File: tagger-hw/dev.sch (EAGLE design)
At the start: 50 parts, among them J2 22-23-2021, J3 22-23-2021, X1 EXC-31B

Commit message: Add current sense resistor, calculations
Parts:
- added RSENS: 1R, adafruit:R-US_R0603
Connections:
- new net VCC_R: C2.1, ICPOW.EN, ICPOW.VIN, RSENS.1
- net VCC: now also RSENS.2; no longer C2.1, ICPOW.EN, ICPOW.VIN
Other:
- moved on the sheet: C2
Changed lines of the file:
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@@
 <grid distance="0.1" unitdist="inch" unit="inch" style="lines" multiple="1" display="no" altdistance="0.01" altunitdist="inch" altunit="inch"/>
 <layers>
-<layer number="1" name="Top" color="4" fill="1" visible="yes" active="no"/>
-<layer number="16" name="Bottom" color="1" fill="1" visible="yes" active="no"/>
-<layer number="17" name="Pads" color="2" fill="1" visible="yes" active="no"/>
-<layer number="18" name="Vias" color="2" fill="1" visible="yes" active="no"/>
-<layer number="19" name="Unrouted" color="6" fill="1" visible="yes" active="no"/>
-<layer number="20" name="Dimension" color="24" fill="1" visible="yes" active="no"/>
-<layer number="21" name="tPlace" color="7" fill="1" visible="yes" active="no"/>
-<layer number="22" name="bPlace" color="7" fill="1" visible="yes" active="no"/>
-<layer number="23" name="tOrigins" color="15" fill="1" visible="yes" active="no"/>
-<layer number="24" name="bOrigins" color="15" fill="1" visible="yes" active="no"/>
-<layer number="25" name="tNames" color="7" fill="1" visible="yes" active="no"/>
-<layer number="26" name="bNames" color="7" fill="1" visible="yes" active="no"/>
-<layer number="27" name="tValues" color="7" fill="1" visible="yes" active="no"/>
-<layer number="28" name="bValues" color="7" fill="1" visible="yes" active="no"/>
+<layer number="1" name="Top" color="4" fill="1" visible="no" active="no"/>
+<layer number="16" name="Bottom" color="1" fill="1" visible="no" active="no"/>
+<layer number="17" name="Pads" color="2" fill="1" visible="no" active="no"/>
+<layer number="18" name="Vias" color="2" fill="1" visible="no" active="no"/>
+<layer number="19" name="Unrouted" color="6" fill="1" visible="no" active="no"/>
+<layer number="20" name="Dimension" color="24" fill="1" visible="no" active="no"/>
+<layer number="21" name="tPlace" color="7" fill="1" visible="no" active="no"/>
+<layer number="22" name="bPlace" color="7" fill="1" visible="no" active="no"/>
+<layer number="23" name="tOrigins" color="15" fill="1" visible="no" active="no"/>
+<layer number="24" name="bOrigins" color="15" fill="1" visible="no" active="no"/>
+<layer number="25" name="tNames" color="7" fill="1" visible="no" active="no"/>
+<layer number="26" name="bNames" color="7" fill="1" visible="no" active="no"/>
+<layer number="27" name="tValues" color="7" fill="1" visible="no" active="no"/>
+<layer number="28" name="bValues" color="7" fill="1" visible="no" active="no"/>
 <layer number="29" name="tStop" color="7" fill="3" visible="no" active="no"/>
 <layer number="30" name="bStop" color="7" fill="6" visible="no" active="no"/>
@@
 <layer number="35" name="tGlue" color="7" fill="4" visible="no" active="no"/>
 <layer number="36" name="bGlue" color="7" fill="5" visible="no" active="no"/>
-<layer number="37" name="tTest" color="7" fill="1" visible="yes" active="no"/>
-<layer number="38" name="bTest" color="7" fill="1" visible="yes" active="no"/>
+<layer number="37" name="tTest" color="7" fill="1" visible="no" active="no"/>
+<layer number="38" name="bTest" color="7" fill="1" visible="no" active="no"/>
 <layer number="39" name="tKeepout" color="4" fill="11" visible="no" active="no"/>
 <layer number="40" name="bKeepout" color="1" fill="11" visible="no" active="no"/>
@@
 <layer number="44" name="Drills" color="7" fill="1" visible="no" active="no"/>
 <layer number="45" name="Holes" color="7" fill="1" visible="no" active="no"/>
-<layer number="46" name="Milling" color="3" fill="1" visible="yes" active="no"/>
-<layer number="47" name="Measures" color="7" fill="1" visible="yes" active="no"/>
-<layer number="48" name="Document" color="7" fill="1" visible="yes" active="no"/>
-<layer number="49" name="Reference" color="7" fill="1" visible="yes" active="no"/>
-<layer number="50" name="dxf" color="7" fill="1" visible="yes" active="no"/>
-<layer number="51" name="tDocu" color="7" fill="1" visible="yes" active="no"/>
-<layer number="52" name="bDocu" color="7" fill="1" visible="yes" active="no"/>
-<layer number="53" name="tGND_GNDA" color="7" fill="9" visible="yes" active="no"/>
-<layer number="54" name="bGND_GNDA" color="1" fill="9" visible="yes" active="no"/>
-<layer number="56" name="wert" color="7" fill="1" visible="yes" active="no"/>
-<layer number="57" name="tCAD" color="7" fill="1" visible="yes" active="no"/>
-<layer number="59" name="tCarbon" color="7" fill="1" visible="yes" active="no"/>
-<layer number="60" name="bCarbon" color="7" fill="1" visible="yes" active="no"/>
+<layer number="46" name="Milling" color="3" fill="1" visible="no" active="no"/>
+<layer number="47" name="Measures" color="7" fill="1" visible="no" active="no"/>
+<layer number="48" name="Document" color="7" fill="1" visible="no" active="no"/>
+<layer number="49" name="Reference" color="7" fill="1" visible="no" active="no"/>
+<layer number="50" name="dxf" color="7" fill="1" visible="no" active="no"/>
+<layer number="51" name="tDocu" color="7" fill="1" visible="no" active="no"/>
+<layer number="52" name="bDocu" color="7" fill="1" visible="no" active="no"/>
+<layer number="53" name="tGND_GNDA" color="7" fill="9" visible="no" active="no"/>
+<layer number="54" name="bGND_GNDA" color="1" fill="9" visible="no" active="no"/>
+<layer number="56" name="wert" color="7" fill="1" visible="no" active="no"/>
+<layer number="57" name="tCAD" color="7" fill="1" visible="no" active="no"/>
+<layer number="59" name="tCarbon" color="7" fill="1" visible="no" active="no"/>
+<layer number="60" name="bCarbon" color="7" fill="1" visible="no" active="no"/>
 <layer number="88" name="SimResults" color="9" fill="1" visible="yes" active="yes"/>
 <layer number="89" name="SimProbes" color="9" fill="1" visible="yes" active="yes"/>
@@
 <part name="+3V15" library="supply1" library_urn="urn:adsk.eagle:library:371" deviceset="+3V3" device=""/>
 <part name="U$1" library="dorskyee" deviceset="MICROSD" device=""/>
+<part name="RSENS" library="adafruit" deviceset="R-US_" device="R0603" value="1R"/>
 </parts>
 <sheets>
@@
 <instance part="+3V3" gate="G$1" x="17.78" y="50.8"/>
 <instance part="ICPOW" gate="G$1" x="129.54" y="38.1" rot="R270"/>
-<instance part="P+2" gate="VCC" x="99.06" y="50.8"/>
+<instance part="P+2" gate="VCC" x="88.9" y="55.88"/>
 <instance part="SUPPLY1" gate="GND" x="111.76" y="22.86"/>
 <instance part="C1" gate="G$1" x="149.86" y="35.56"/>
 <instance part="SUPPLY5" gate="GND" x="149.86" y="22.86"/>
-<instance part="C2" gate="G$1" x="99.06" y="35.56"/>
-<instance part="SUPPLY4" gate="GND" x="99.06" y="22.86"/>
+<instance part="C2" gate="G$1" x="104.14" y="33.02"/>
+<instance part="SUPPLY4" gate="GND" x="104.14" y="22.86"/>
 <instance part="SUPPLY8" gate="GND" x="7.62" y="33.02"/>
 <instance part="ACT" gate="G$1" x="-73.66" y="60.96"/>
@@
 <instance part="+3V15" gate="G$1" x="22.86" y="-114.3"/>
 <instance part="U$1" gate="G$1" x="66.04" y="73.66"/>
+<instance part="RSENS" gate="G$1" x="96.52" y="43.18" rot="R180"/>
 </instances>
 <busses>
@@
 <pinref part="C2" gate="G$1" pin="2"/>
 <pinref part="SUPPLY4" gate="GND" pin="GND"/>
-<wire x1="99.06" y1="25.4" x2="99.06" y2="30.48" width="0.1524" layer="91"/>
+<wire x1="104.14" y1="25.4" x2="104.14" y2="27.94" width="0.1524" layer="91"/>
 </segment>
 <segment>
@@
 <net name="VCC" class="0">
 <segment>
-<wire x1="114.3" y1="43.18" x2="109.22" y2="43.18" width="0.1524" layer="91"/>
-<wire x1="109.22" y1="43.18" x2="99.06" y2="43.18" width="0.1524" layer="91"/>
-<wire x1="99.06" y1="43.18" x2="99.06" y2="48.26" width="0.1524" layer="91"/>
-<pinref part="ICPOW" gate="G$1" pin="VIN"/>
 <pinref part="P+2" gate="VCC" pin="VCC"/>
-<pinref part="C2" gate="G$1" pin="1"/>
-<wire x1="99.06" y1="43.18" x2="99.06" y2="38.1" width="0.1524" layer="91"/>
-<junction x="99.06" y="43.18"/>
-<pinref part="ICPOW" gate="G$1" pin="EN"/>
-<wire x1="114.3" y1="33.02" x2="109.22" y2="33.02" width="0.1524" layer="91"/>
-<wire x1="109.22" y1="33.02" x2="109.22" y2="43.18" width="0.1524" layer="91"/>
-<junction x="109.22" y="43.18"/>
+<wire x1="88.9" y1="53.34" x2="88.9" y2="43.18" width="0.1524" layer="91"/>
+<pinref part="RSENS" gate="G$1" pin="2"/>
+<wire x1="91.44" y1="43.18" x2="88.9" y2="43.18" width="0.1524" layer="91"/>
 </segment>
 <segment>
@@
 </segment>
 </net>
+<net name="VCC_R" class="0">
+<segment>
+<wire x1="114.3" y1="43.18" x2="109.22" y2="43.18" width="0.1524" layer="91"/>
+<pinref part="ICPOW" gate="G$1" pin="VIN"/>
+<pinref part="ICPOW" gate="G$1" pin="EN"/>
+<wire x1="114.3" y1="33.02" x2="109.22" y2="33.02" width="0.1524" layer="91"/>
+<wire x1="109.22" y1="33.02" x2="109.22" y2="43.18" width="0.1524" layer="91"/>
+<junction x="109.22" y="43.18"/>
+<label x="106.68" y="45.72" size="1.778" layer="95"/>
+<pinref part="RSENS" gate="G$1" pin="1"/>
+<wire x1="101.6" y1="43.18" x2="104.14" y2="43.18" width="0.1524" layer="91"/>
+<pinref part="C2" gate="G$1" pin="1"/>
+<wire x1="104.14" y1="35.56" x2="104.14" y2="43.18" width="0.1524" layer="91"/>
+<wire x1="104.14" y1="43.18" x2="109.22" y2="43.18" width="0.1524" layer="91"/>
+<junction x="104.14" y="43.18"/>
+</segment>
+</net>

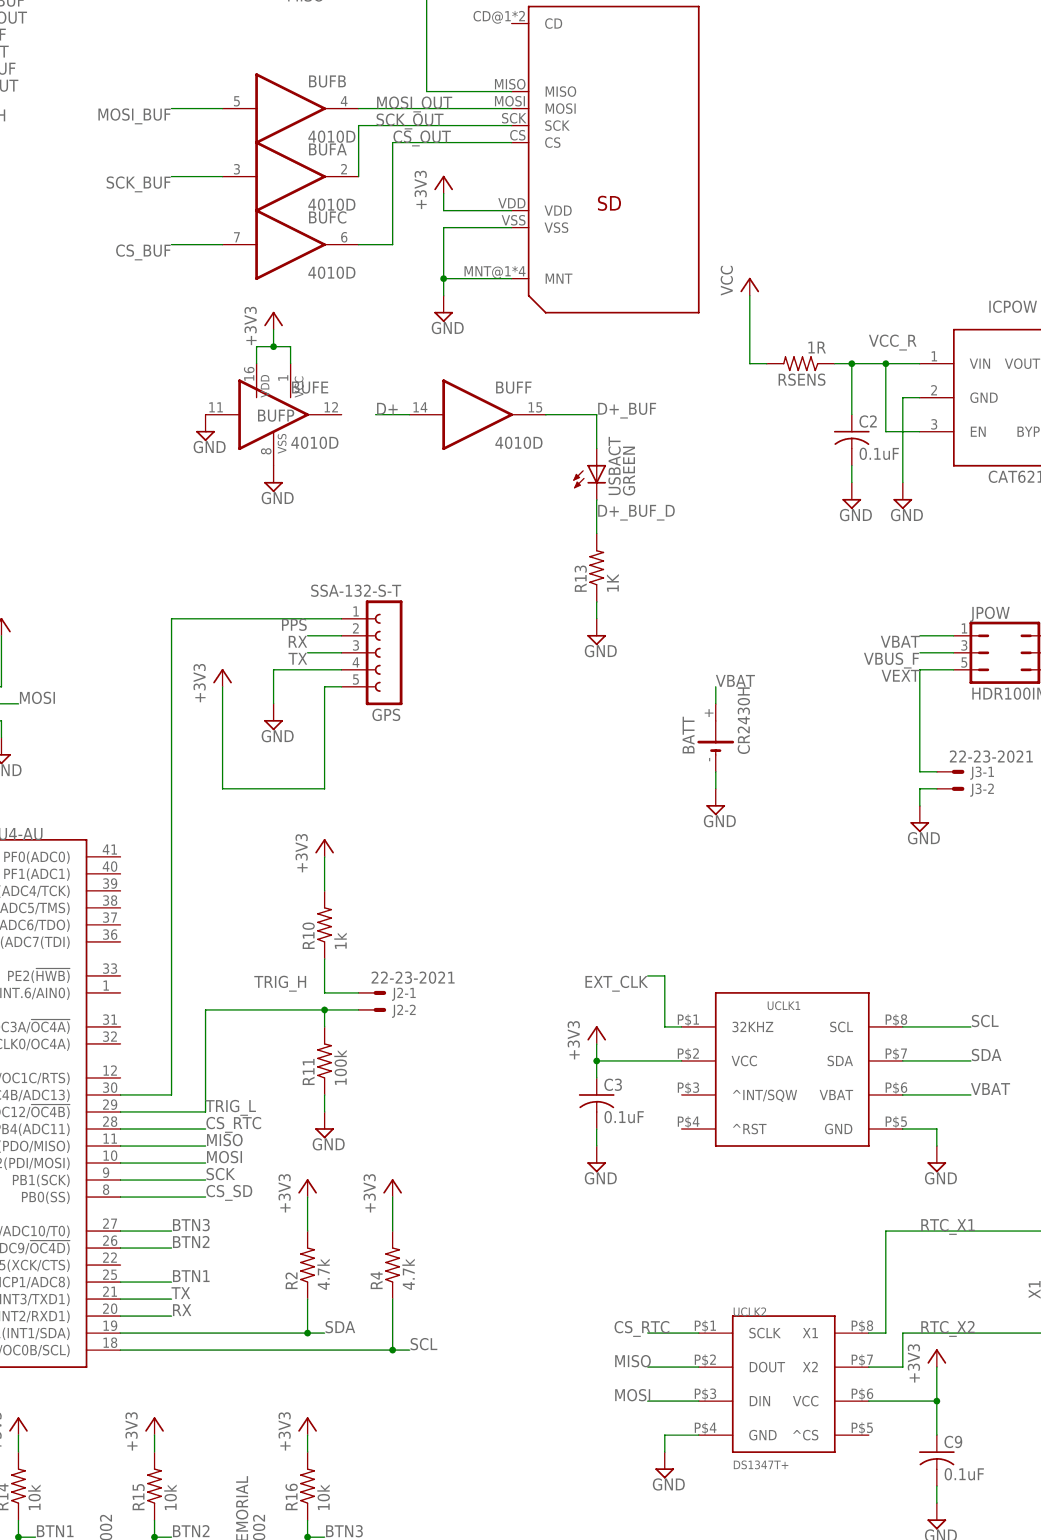
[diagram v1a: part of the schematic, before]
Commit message: Add some test points
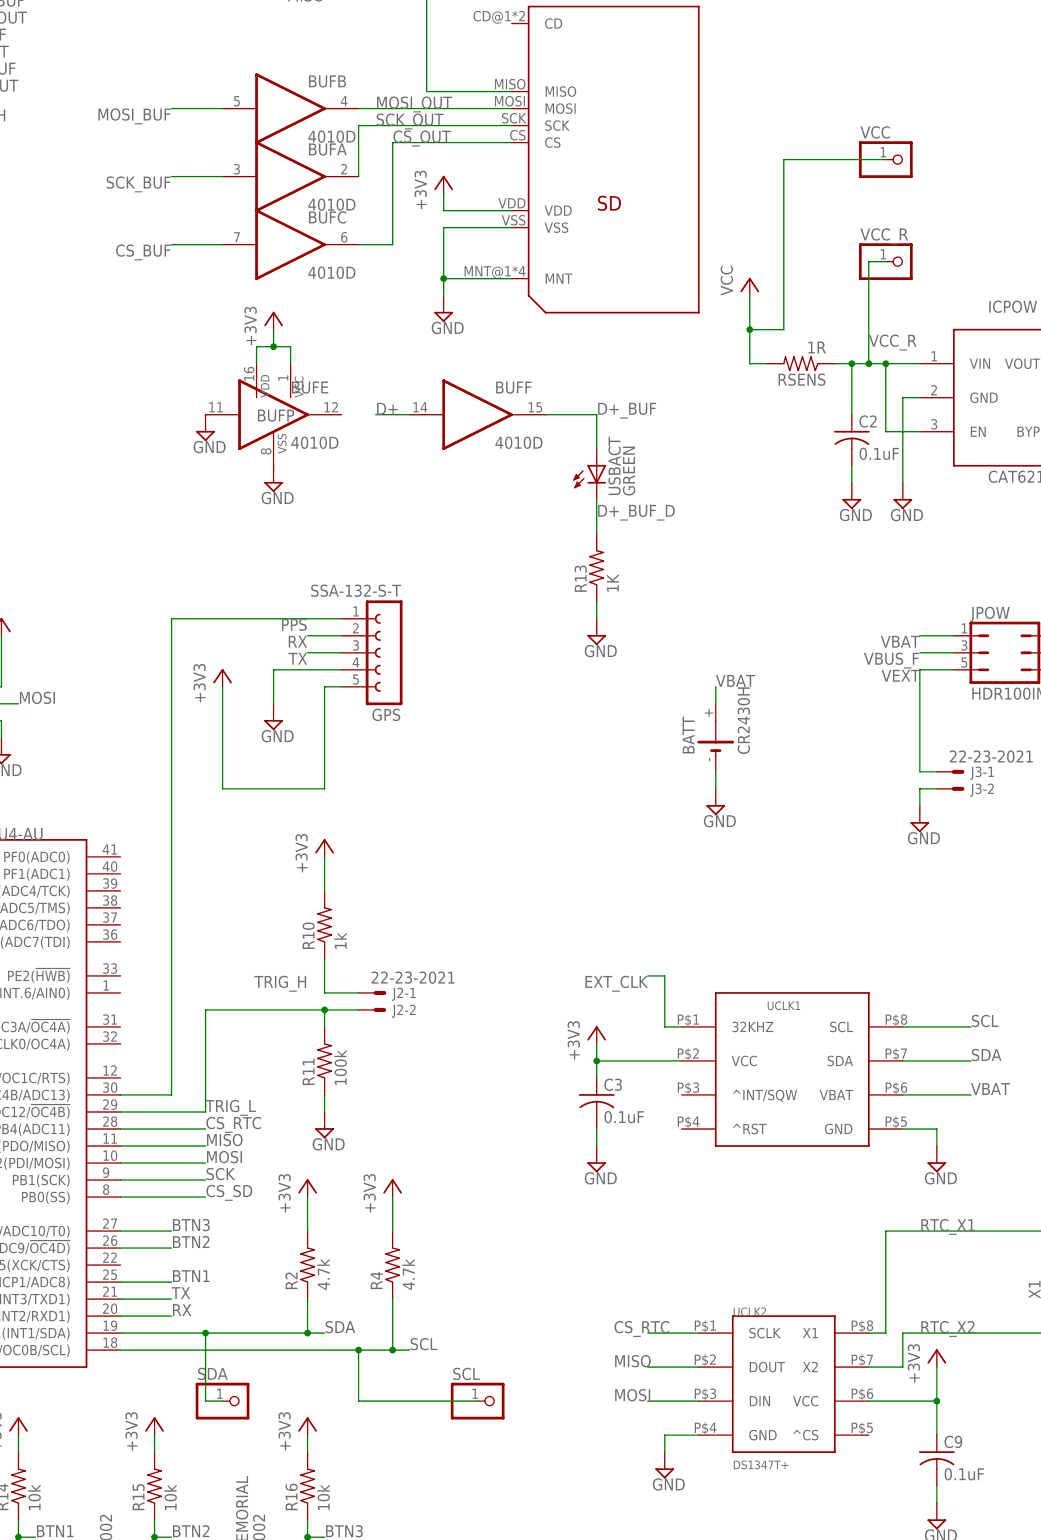
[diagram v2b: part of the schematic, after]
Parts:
- added SCL, SDA, VCC, VCC_R: (no value), adafruit:PINHD-1X1
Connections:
- net SCL: now also SCL.1
- net SDA: now also SDA.1
- net VCC: now also VCC.1
- net VCC_R: now also VCC_R.1
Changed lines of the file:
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@@
 <part name="U$1" library="dorskyee" deviceset="MICROSD" device=""/>
 <part name="RSENS" library="adafruit" deviceset="R-US_" device="R0603" value="1R"/>
+<part name="VCC_R" library="adafruit" deviceset="PINHD-1X1" device=""/>
+<part name="VCC" library="adafruit" deviceset="PINHD-1X1" device=""/>
+<part name="SDA" library="adafruit" deviceset="PINHD-1X1" device=""/>
+<part name="SCL" library="adafruit" deviceset="PINHD-1X1" device=""/>
 </parts>
 <sheets>
@@
 <instance part="U$1" gate="G$1" x="66.04" y="73.66"/>
 <instance part="RSENS" gate="G$1" x="96.52" y="43.18" rot="R180"/>
+<instance part="VCC_R" gate="G$1" x="111.76" y="58.42"/>
+<instance part="VCC" gate="G$1" x="111.76" y="73.66"/>
+<instance part="SDA" gate="G$1" x="12.7" y="-111.76"/>
+<instance part="SCL" gate="G$1" x="50.8" y="-111.76"/>
 </instances>
 <busses>
@@
 <segment>
 <pinref part="P+2" gate="VCC" pin="VCC"/>
-<wire x1="88.9" y1="53.34" x2="88.9" y2="43.18" width="0.1524" layer="91"/>
+<wire x1="88.9" y1="53.34" x2="88.9" y2="48.26" width="0.1524" layer="91"/>
 <pinref part="RSENS" gate="G$1" pin="2"/>
+<wire x1="88.9" y1="48.26" x2="88.9" y2="43.18" width="0.1524" layer="91"/>
 <wire x1="91.44" y1="43.18" x2="88.9" y2="43.18" width="0.1524" layer="91"/>
+<pinref part="VCC" gate="G$1" pin="1"/>
+<wire x1="109.22" y1="73.66" x2="93.98" y2="73.66" width="0.1524" layer="91"/>
+<wire x1="93.98" y1="73.66" x2="93.98" y2="48.26" width="0.1524" layer="91"/>
+<wire x1="93.98" y1="48.26" x2="88.9" y2="48.26" width="0.1524" layer="91"/>
+<junction x="88.9" y="48.26"/>
 </segment>
 <segment>
@@
 <pinref part="UC" gate="G$1" pin="PD0(INT0/OC0B/SCL)"/>
 <label x="38.1" y="-104.14" size="1.778" layer="95"/>
-<wire x1="-5.08" y1="-104.14" x2="35.56" y2="-104.14" width="0.1524" layer="91"/>
+<wire x1="-5.08" y1="-104.14" x2="30.48" y2="-104.14" width="0.1524" layer="91"/>
+<wire x1="30.48" y1="-104.14" x2="35.56" y2="-104.14" width="0.1524" layer="91"/>
 <wire x1="35.56" y1="-104.14" x2="35.56" y2="-96.52" width="0.1524" layer="91"/>
 <pinref part="R4" gate="G$1" pin="1"/>
 <wire x1="35.56" y1="-104.14" x2="38.1" y2="-104.14" width="0.1524" layer="91"/>
 <junction x="35.56" y="-104.14"/>
+<pinref part="SCL" gate="G$1" pin="1"/>
+<wire x1="48.26" y1="-111.76" x2="30.48" y2="-111.76" width="0.1524" layer="91"/>
+<wire x1="30.48" y1="-111.76" x2="30.48" y2="-104.14" width="0.1524" layer="91"/>
+<junction x="30.48" y="-104.14"/>
 </segment>
 </net>
@@
 <label x="25.4" y="-101.6" size="1.778" layer="95"/>
 <pinref part="R2" gate="G$1" pin="1"/>
-<wire x1="-5.08" y1="-101.6" x2="22.86" y2="-101.6" width="0.1524" layer="91"/>
+<wire x1="-5.08" y1="-101.6" x2="7.62" y2="-101.6" width="0.1524" layer="91"/>
+<wire x1="7.62" y1="-101.6" x2="22.86" y2="-101.6" width="0.1524" layer="91"/>
 <wire x1="22.86" y1="-101.6" x2="22.86" y2="-96.52" width="0.1524" layer="91"/>
 <wire x1="22.86" y1="-101.6" x2="25.4" y2="-101.6" width="0.1524" layer="91"/>
 <junction x="22.86" y="-101.6"/>
+<pinref part="SDA" gate="G$1" pin="1"/>
+<wire x1="10.16" y1="-111.76" x2="7.62" y2="-111.76" width="0.1524" layer="91"/>
+<wire x1="7.62" y1="-111.76" x2="7.62" y2="-101.6" width="0.1524" layer="91"/>
+<junction x="7.62" y="-101.6"/>
 </segment>
 </net>
@@
 <pinref part="C2" gate="G$1" pin="1"/>
 <wire x1="104.14" y1="35.56" x2="104.14" y2="43.18" width="0.1524" layer="91"/>
-<wire x1="104.14" y1="43.18" x2="109.22" y2="43.18" width="0.1524" layer="91"/>
+<wire x1="104.14" y1="43.18" x2="106.68" y2="43.18" width="0.1524" layer="91"/>
 <junction x="104.14" y="43.18"/>
-</segment>
-</net>
+<pinref part="VCC_R" gate="G$1" pin="1"/>
+<wire x1="106.68" y1="43.18" x2="109.22" y2="43.18" width="0.1524" layer="91"/>
+<wire x1="109.22" y1="58.42" x2="106.68" y2="58.42" width="0.1524" layer="91"/>
+<wire x1="106.68" y1="58.42" x2="106.68" y2="43.18" width="0.1524" layer="91"/>
+<junction x="106.68" y="43.18"/>
+</segment>
+</net>
